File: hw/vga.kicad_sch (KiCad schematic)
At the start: 23 parts, among them J2 DB15_Female_HighDensity_Mount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, P2 COLOR_SELECT, P4 CONN_01X02, P5 CLOCK_SELECT, U1 74HC4053, U2 23LCV512, U3 NB3N502, Y1 10MHz

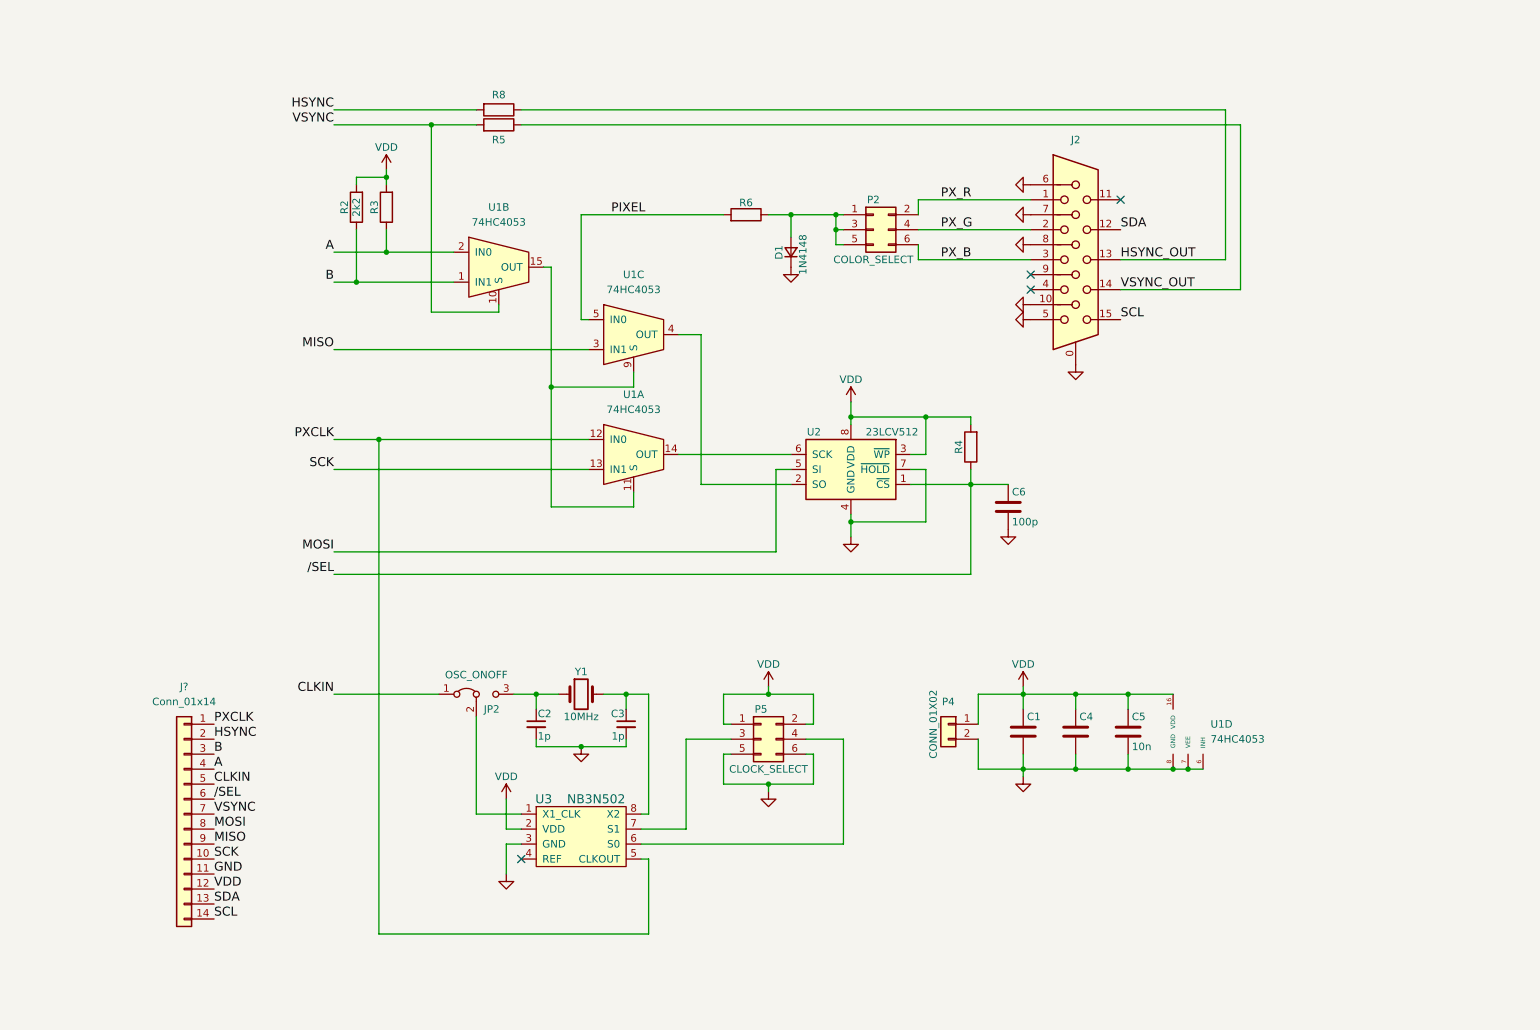
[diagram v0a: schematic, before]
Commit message: Changed PLL chip to ICS501 and removed onboard oscillator option. Changed J1 footprint to 14 pin double row pin header. Swapped J1 pins 2 and 3 (hsync and B). J1 pin 1 is now ground (used to be pixel clock out). B line now has pulldown (used to be pullup). Rerouted the board for lower EMC (but still 2 layers).
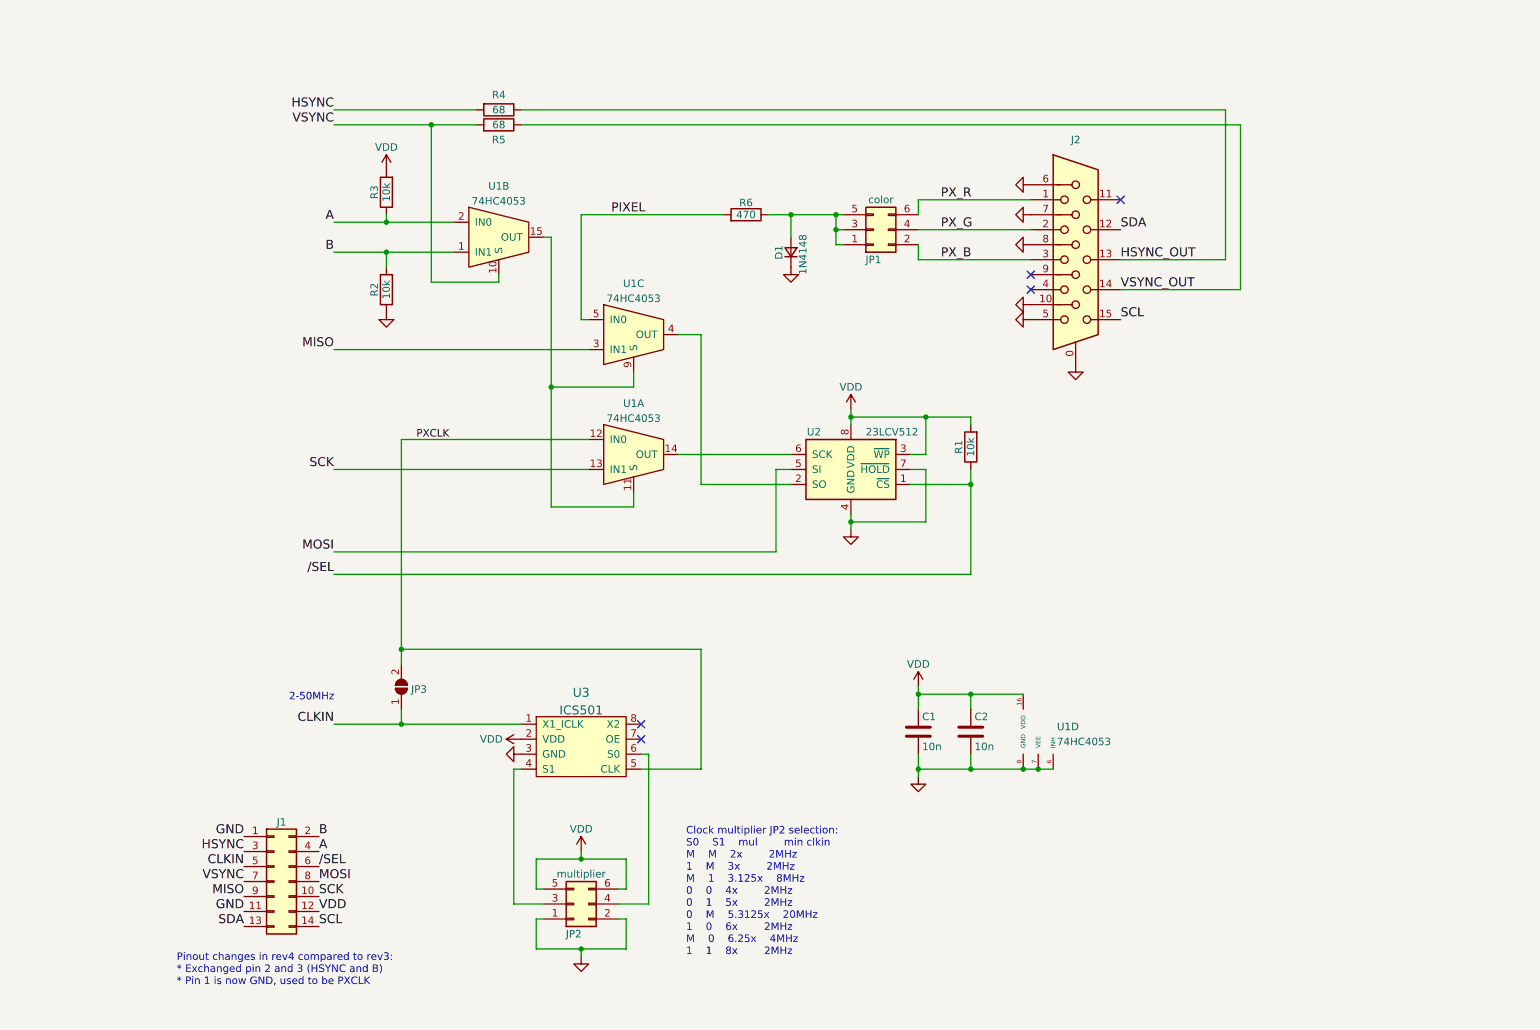
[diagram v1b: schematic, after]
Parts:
- removed C1: (no value), symbol Device:C
- removed C2, C3: 1p, Capacitors_SMD:C_0805, symbol Device:C_Small
- removed C6: 100p, Capacitors_SMD:C_0805, symbol Device:C
- removed J?: Conn_01x14, symbol Connector_Generic:Conn_01x14
- removed JP2: OSC_ONOFF, Pin_Headers:Pin_Header_Straight_1x03, symbol Jumper:Jumper_3_Bridged12
- removed P4: CONN_01X02, Pin_Headers:Pin_Header_Straight_1x02, symbol Connector_Generic:Conn_01x02
- removed U3: NB3N502, Package_SO:SO-8_3.9x4.9mm_P1.27mm, symbol vga:NB3N502
- removed Y1: 10MHz, Crystals:Crystal_SMD_5032_2Pads, symbol Device:Crystal
- added J1: Conn_02x07_Odd_Even, Connector_IDC:IDC-Header_2x07_P2.54mm_Vertical, symbol Connector_Generic:Conn_02x07_Odd_Even
- added JP3: SolderJumper_2_Open, Jumper:SolderJumper-2_P1.3mm_Open_RoundedPad1.0x1.5mm, symbol Jumper:SolderJumper_2_Open
- added U3: ICS501, Package_SO:SO-8_3.9x4.9mm_P1.27mm, symbol vga:ICS501
- C1: renamed from C4; value (none) -> 10n; footprint (none) -> Capacitor_SMD:C_0805_2012Metric
- C2: renamed from C5; footprint Capacitors_SMD:C_0805 -> Capacitor_SMD:C_0805_2012Metric
- D1: footprint Diodes_SMD:SOD-323_HandSoldering -> Diode_SMD:D_SOD-323_HandSoldering
- J2: MFG Name (none) -> CONNFLY; MFG Part Num (none) -> DS1038-15FBNSIA74-0CC; TME PN (none) -> DMR15F-HD
- JP1: renamed from P2; value COLOR_SELECT -> color; MFG Name (none) -> Amphenol; MFG Part Num (none) -> 67996-206HLF; TME PN (none) -> 67996-206HLF
- JP2: renamed from P5; value CLOCK_SELECT -> multiplier; MFG Name (none) -> Amphenol; MFG Part Num (none) -> 67996-206HLF; TME PN (none) -> 67996-206HLF
- R1: renamed from R4; value (none) -> 10k; footprint (none) -> Resistor_SMD:R_0805_2012Metric
- R2: value 2k2 -> 10k; footprint Resistors_SMD:R_0805 -> Resistor_SMD:R_0805_2012Metric
- R3: value (none) -> 10k; footprint (none) -> Resistor_SMD:R_0805_2012Metric
- R4: renamed from R8; value (none) -> 68; footprint (none) -> Resistor_SMD:R_0805_2012Metric
- R5: value (none) -> 68; footprint (none) -> Resistor_SMD:R_0805_2012Metric
- R6: value (none) -> 470; footprint (none) -> Resistor_SMD:R_0805_2012Metric
- U1: MFG Name (none) -> NEXPERIA; MFG Part Num (none) -> 74HC4053D,653; TME PN (none) -> 74HC4053D.653
- U2: Farnell PN (none) -> 23LCV512-I/SN; MFG Name (none) -> MICROCHIP TECHNOLOGY; MFG Part Num (none) -> 23LCV512-I/SN; TME PN (none) -> 23LCV512-I/SN
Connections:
- net /SEL: now also J1.6 (Pin_6)
- net A: now also J1.4 (Pin_4)
- net B: now also R2.2, J1.2 (Pin_2); no longer R2.1
- net CLKIN: now also J1.5 (Pin_5), JP3.1 (A), U3.1 (X1_ICLK)
- net GND: now also JP2.1 (Pin_1), JP2.2 (Pin_2), R2.1, J1.1 (Pin_1), J1.11 (Pin_11), U3.3 (GND); no longer JP2.5 (Pin_5), JP2.6 (Pin_6)
- net HSYNC: now also J1.3 (Pin_3)
- net MISO: now also J1.9 (Pin_9)
- net MOSI: now also J1.8 (Pin_8)
- net PXCLK: now also JP3.2 (B), U3.5 (CLK)
- net PX_B: now also JP1.2 (Pin_2); no longer JP1.6 (Pin_6)
- net PX_R: now also JP1.6 (Pin_6); no longer JP1.2 (Pin_2)
- net SCK: now also J1.10 (Pin_10)
- net SCL: now also J1.14 (Pin_14)
- net SDA: now also J1.13 (Pin_13)
- net VDD: now also JP2.5 (Pin_5), JP2.6 (Pin_6), J1.12 (Pin_12), U3.2 (VDD); no longer JP2.1 (Pin_1), JP2.2 (Pin_2), R2.2
- net VSYNC: now also J1.7 (Pin_7)
- net at JP2.4 (Pin_4): now also U3.6 (S0)
- net at JP2.3 (Pin_3): now also U3.4 (S1)
- no-connect marks 4 -> 5
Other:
- note added: "2-50MHz"
- note added: "Clock multiplier JP2 selection: S0 S1 mul min clkin M M 2x 2MHz 1 M 3x 2MHz M 1 3.125x 8MHz 0 0 4x 2MHz 0 1 5x 2MHz 0 M 5.3125x 20MHz 1 0 6x 2MHz M 0 6.25x 4MHz 1 1 8x 2MHz"
- note added: "Pinout changes in rev4 compared to rev3: * Exchanged pin 2 and 3 (HSYNC and B) * Pin 1 is now GND, used to be PXCLK"
- moved on the sheet: C1, C2, JP2, R2, R3, U1B, U1D

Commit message: Reduced J1 to 10pins by removing all non-essential pins. Reviewed comments on the schematic. Added solder jumper so that more PLL chips could be used. Changed AB input to use pullups like rev3 did (but with 4x higher value). Finished board layout.
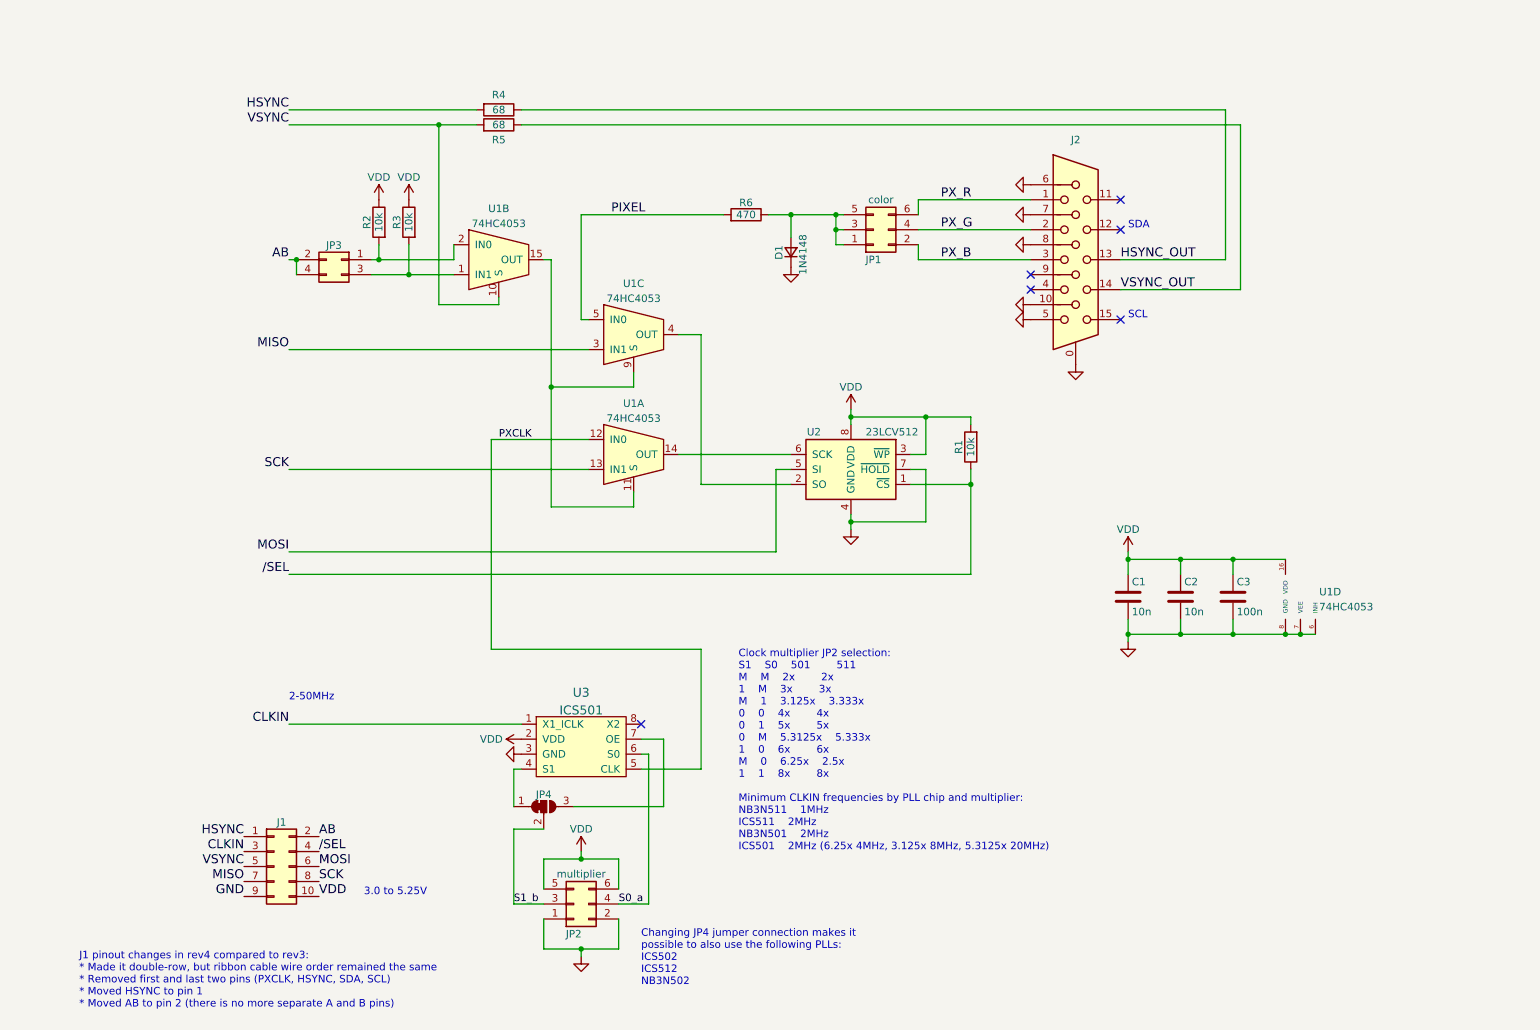
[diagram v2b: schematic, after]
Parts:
- removed J1: Conn_02x07_Odd_Even, Connector_IDC:IDC-Header_2x07_P2.54mm_Vertical, symbol Connector_Generic:Conn_02x07_Odd_Even
- removed JP3: SolderJumper_2_Open, Jumper:SolderJumper-2_P1.3mm_Open_RoundedPad1.0x1.5mm, symbol Jumper:SolderJumper_2_Open
- added C3: 100n, Capacitor_SMD:C_0805_2012Metric, symbol Device:C
- added J1: Conn_02x05_Odd_Even, Connector_IDC:IDC-Header_2x05_P2.54mm_Vertical, symbol Connector_Generic:Conn_02x05_Odd_Even
- added JP3: Conn_02x02_Odd_Even, Connector_PinHeader_2.54mm:PinHeader_2x02_P2.54mm_Vertical, symbol Connector_Generic:Conn_02x02_Odd_Even
- added JP4: SolderJumper_3_Bridged12, Jumper:SolderJumper-3_P1.3mm_Open_RoundedPad1.0x1.5mm, symbol Jumper:SolderJumper_3_Bridged12
- JP1, JP2: footprint Pin_Headers:Pin_Header_Straight_2x03 -> Connector_PinHeader_2.54mm:PinHeader_2x03_P2.54mm_Vertical
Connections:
- net /SEL: now also J1.4 (Pin_4)
- net CLKIN: now also J1.3 (Pin_3)
- net GND: now also C3.2, J1.9 (Pin_9); no longer R2.1
- net HSYNC: now also J1.1 (Pin_1)
- net MISO: now also J1.7 (Pin_7)
- net MOSI: now also J1.6 (Pin_6)
- net SCK: now also J1.8 (Pin_8)
- net VDD: now also R2.1, R3.1, C3.1, J1.10 (Pin_10); no longer R3.2
- net VSYNC: now also J1.5 (Pin_5)
- net at U3.4 (S1): now also JP4.1 (A); no longer JP2.3 (Pin_3)
- net S0_a: now reaches JP2.4 (Pin_4), U3.6 (S0)
- net at U3.7 (OE): now also JP4.3 (B)
- net A: no longer names the net of U1.2 (IN0)
- net A: now also R2.2, JP3.1 (Pin_1); no longer R3.1
- net B: no longer names the net of U1.1 (IN1)
- net B: now also R3.2, JP3.3 (Pin_3); no longer R2.2
- net SCL: no longer names the net of J2.15
- net SDA: no longer names the net of J2.12
- new net AB: J1.2 (Pin_2), JP3.2 (Pin_2), JP3.4 (Pin_4)
- new net S1_b: JP2.3 (Pin_3), JP4.2 (C)
- no-connect marks 5 -> 6
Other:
- note added: "3.0 to 5.25V"
- note added: "Changing JP4 jumper connection makes it possible to also use the following PLLs: ICS502 ICS512 NB3N502"
- note added: "Clock multiplier JP2 selection: S1 S0 501 511 M M 2x 2x 1 M 3x 3x M 1 3.125x 3.333x 0 0 4x 4x 0 1 5x 5x 0 M 5.3125x 5.333x 1 0 6x 6x M 0 6.25x 2.5x 1 1 8x 8x Minimum CLKIN frequencies by PLL chip and multiplier: NB3N511 1MHz ICS511 2MHz NB3N501 2MHz ICS501 2MHz (6.25x 4MHz, 3.125x 8MHz, 5.3125x 20MHz)"
- note added: "J1 pinout changes in rev4 compared to rev3: * Made it double-row, but ribbon cable wire order remained the same * Removed first and last two pins (PXCLK, HSYNC, SDA, SCL) * Moved HSYNC to pin 1 * Moved AB to pin 2 (there is no more separate A and B pins)"
- note added: "SCL"
- note added: "SDA"
- note removed: "Clock multiplier JP2 selection: S0 S1 mul min clkin M M 2x 2MHz 1 M 3x 2MHz M 1 3.125x 8MHz 0 0 4x 2MHz 0 1 5x 2MHz 0 M 5.3125x 20MHz 1 0 6x 2MHz M 0 6.25x 4MHz 1 1 8x 2MHz"
- note removed: "Pinout changes in rev4 compared to rev3: * Exchanged pin 2 and 3 (HSYNC and B) * Pin 1 is now GND, used to be PXCLK"
- moved on the sheet: C1, C2, R2, U1B, U1D
